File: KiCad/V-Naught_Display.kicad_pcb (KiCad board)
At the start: 2 copper layers, 70 x 35 mm, 28 parts, among them J1 USB_B_Micro, J2 I2C Header 1, J3 Conn_01x03, J4 Conn_01x02, J5 SWD Header, J6 I2C Header 2, SW1 SW_SPST, SW2 SW_SPST, SW3 SW_SPST, SW4 SW_SPST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

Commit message: Encoder Common pin change from 3v3 to Ground
Need to change encoder center pin to Ground (from 3V3) to allow for pullups to work for pin change detection.
Also, adding working configs for both the Encoder and Button options
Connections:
- SW7 pad C: +3V3 -> GND
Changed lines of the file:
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@@
     (add_net Kill_Switch)
     (add_net NeoPixel)
+    (add_net "Net-(D1-Pad2)")
     (add_net "Net-(D1-Pad4)")
+    (add_net "Net-(J5-Pad6)")
+    (add_net "Net-(J5-Pad7)")
+    (add_net "Net-(J5-Pad8)")
+    (add_net "Net-(J5-Pad9)")
+    (add_net "Net-(U1-Pad4)")
+    (add_net "Net-(U2-Pad12)")
+    (add_net "Net-(U2-Pad13)")
+    (add_net "Net-(U2-Pad14)")
     (add_net SCL)
     (add_net SDA)
@@
       (net 10 Button_Left))
     (pad C thru_hole circle (at 0 7.5) (size 2 2) (drill 1.1) (layers *.Cu *.Mask)
-      (net 3 +3V3))
+      (net 1 GND))
     (pad B thru_hole circle (at 2.5 7.5) (size 2 2) (drill 1.1) (layers *.Cu *.Mask)
       (net 9 Button_Down))

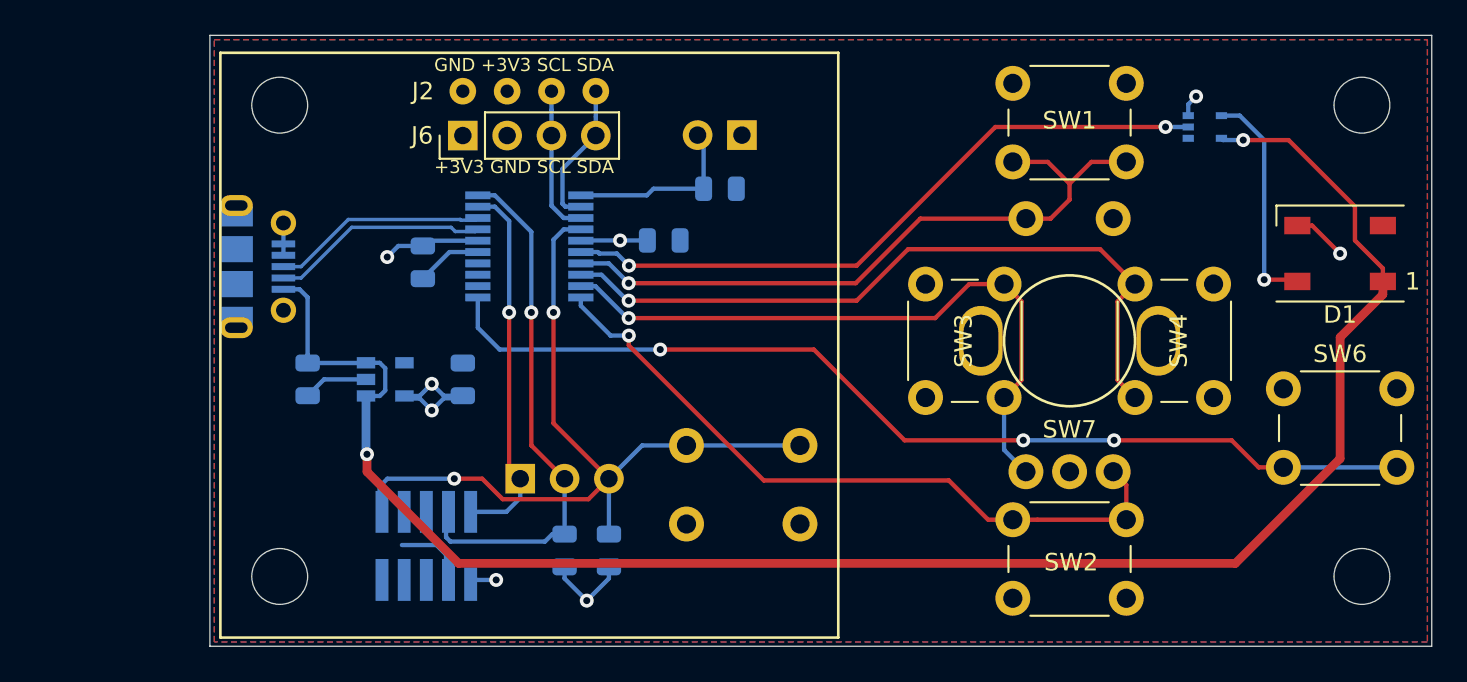
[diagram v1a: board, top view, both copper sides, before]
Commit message: Widen to allow for screw mounting on all 4 sides.
2 screws were deemed insufficient ... =P
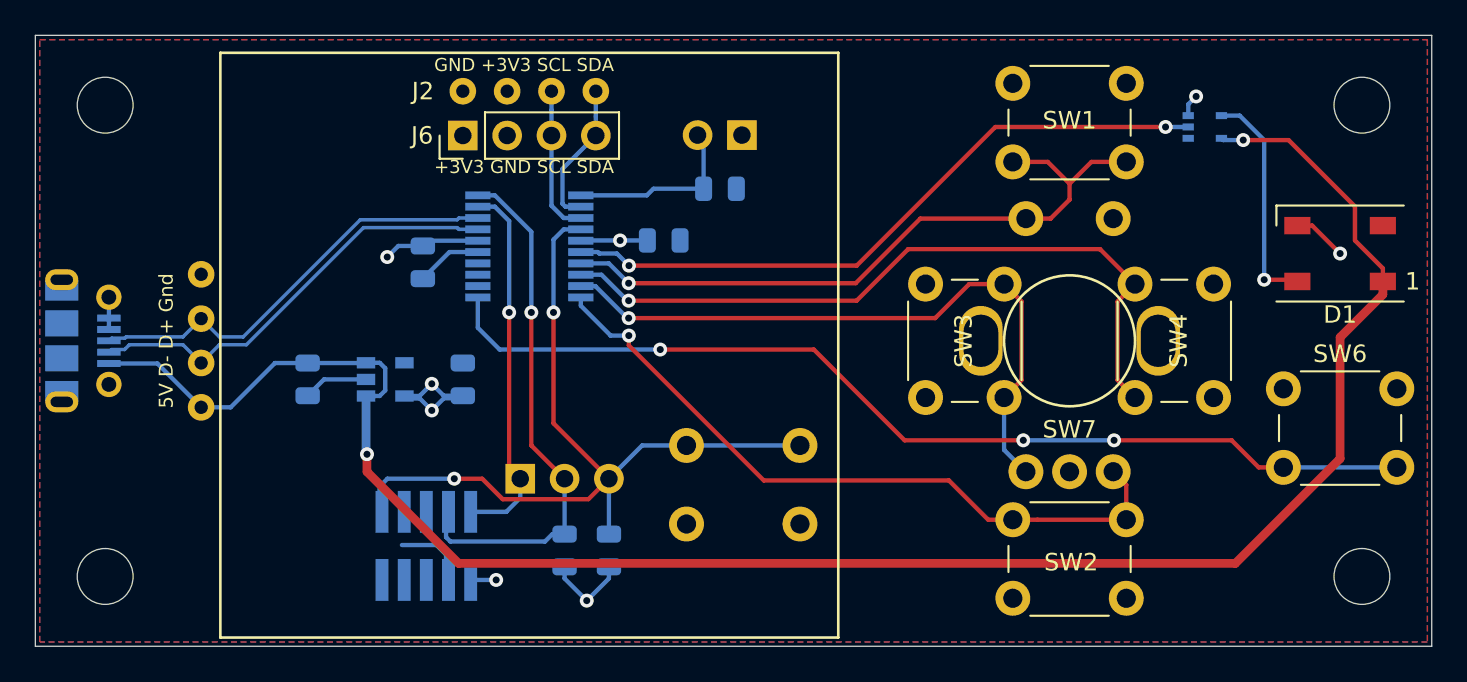
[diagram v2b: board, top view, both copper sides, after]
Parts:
- added J7: USB_Header, TRA_KiCad_Footprints:01x04_unpopulated, B.Cu at (94.7, 67.2)
- SW7: footprint TRA_KiCad_Footprints:EN11 Encoder -> TRA_KiCad_Footprints:EN11_Encoder
- moved J1 10.9 mm to (87.9, 67.2)
- moved H1 10.0 mm to (89.2, 53.6)
- moved H4 10.0 mm to (89.2, 80.7)
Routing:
- net D+: track 12.3 -> 24.9 mm
- net D-: track 12.5 -> 25.0 mm
- net VBUS: track 102.6 -> 110.7 mm
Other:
- board size 70 x 35 mm -> 80 x 35 mm
- board text added: "5V D- D+ Gnd"
- board text added: "Gnd D+ D- 5V"
